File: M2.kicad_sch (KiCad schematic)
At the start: 59 parts, among them J100 Bus_M.2_2199230-2, J6 Bus_M.2_1-2199230-6, Y1 Oscillator_32.768kHz_ECS_2520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

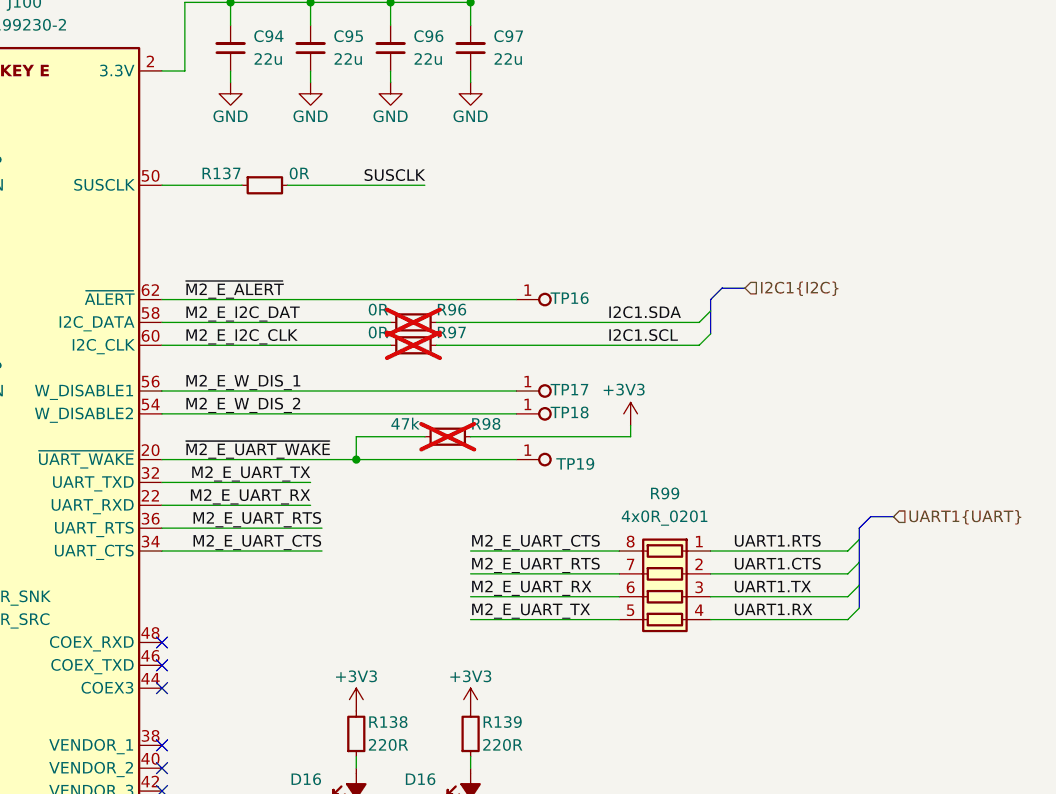
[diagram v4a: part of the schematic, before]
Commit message: [#82048] Beautify M.2 schematic
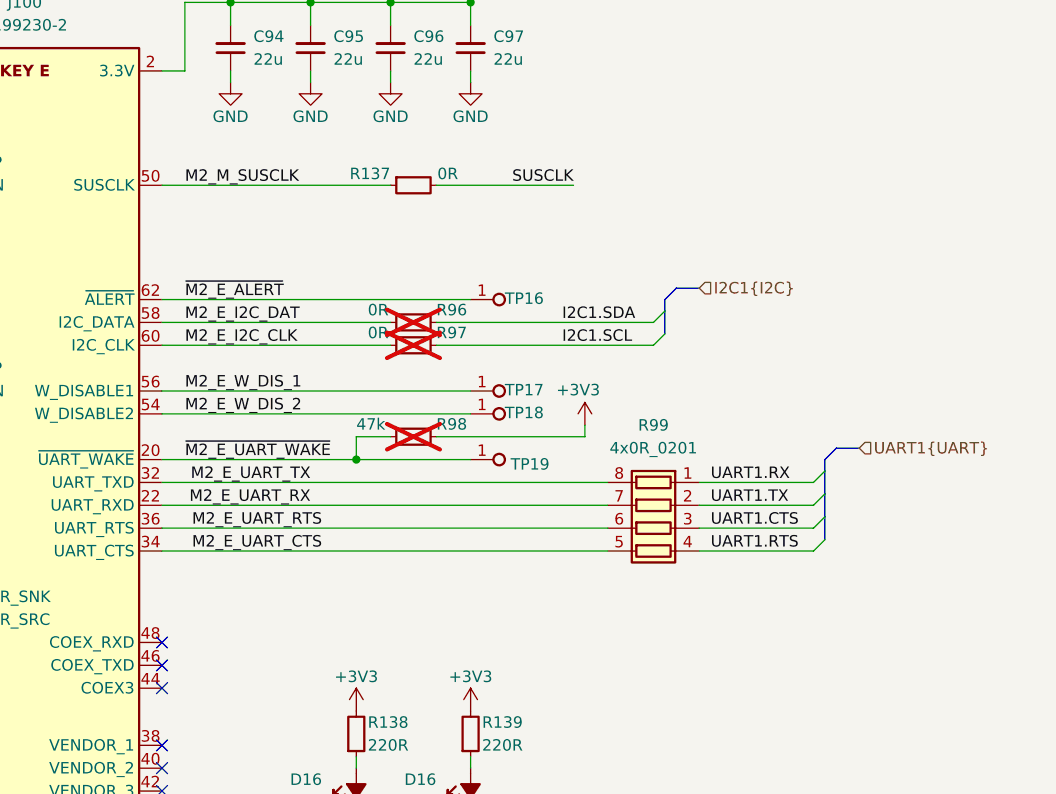
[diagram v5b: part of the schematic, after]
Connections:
- net M2_E_UART_CTS: now also R99.5 (R4.2); no longer R99.8 (R1.2)
- net M2_E_UART_RTS: now also R99.6 (R3.2); no longer R99.7 (R2.2)
- net M2_E_UART_RX: now also R99.7 (R2.2); no longer R99.6 (R3.2)
- net M2_E_UART_TX: now also R99.8 (R1.2); no longer R99.5 (R4.2)
- net M2_M_SUSCLK: now also J100.50 (SUSCLK), R137.1
- net UART1.CTS: now also R99.3 (R3.1); no longer R99.2 (R2.1)
- net UART1.RTS: now also R99.4 (R4.1); no longer R99.1 (R1.1)
- net UART1.RX: now also R99.1 (R1.1); no longer R99.4 (R4.1)
- net UART1.TX: now also R99.2 (R2.1); no longer R99.3 (R3.1)
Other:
- moved on the sheet: R137, R98, R99, TP16, TP17, TP18, TP19

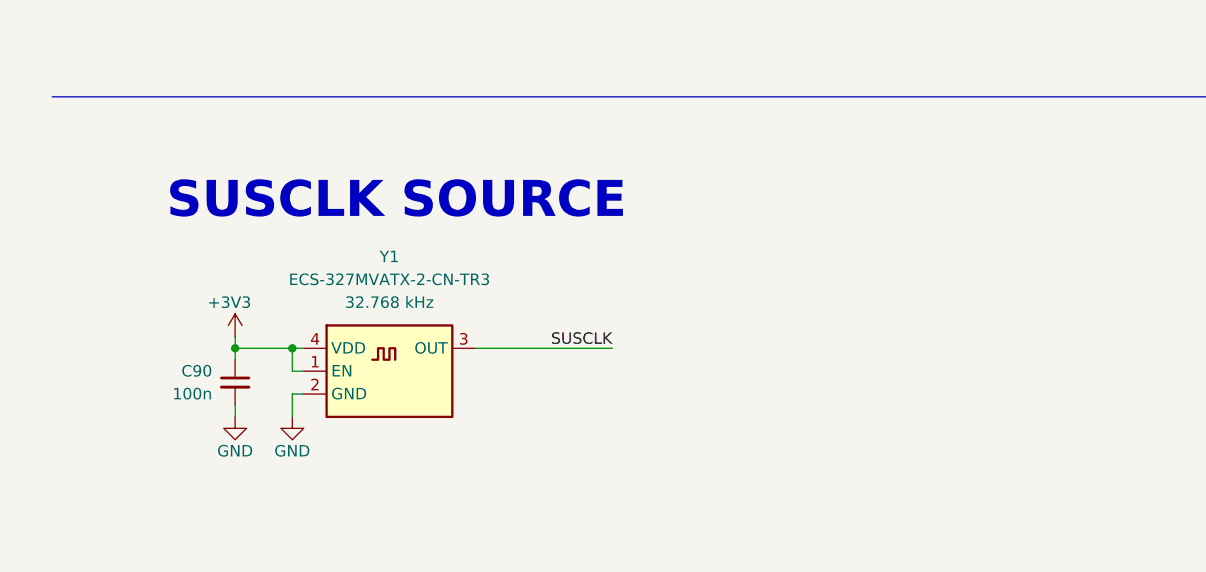
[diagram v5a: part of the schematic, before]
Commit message: [#81970] Connect SFI to SOM
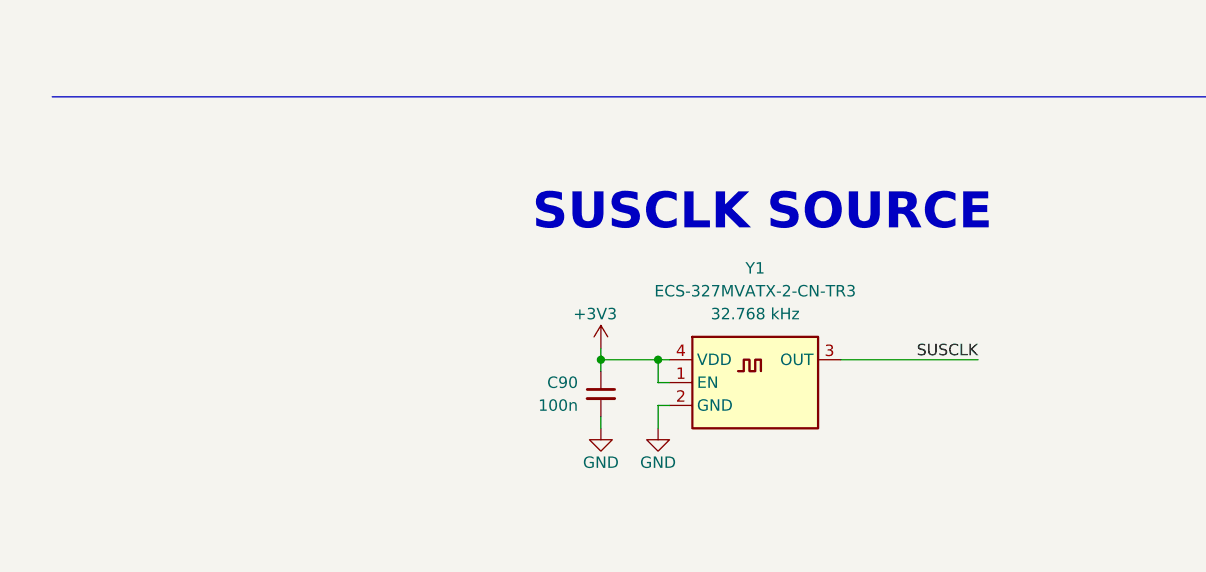
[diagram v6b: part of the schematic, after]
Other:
- moved on the sheet: C90, Y1
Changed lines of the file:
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@@
 	(text "SUSCLK SOURCE"
 		(exclude_from_sim no)
-		(at 25.4 247.65 0)
+		(at 66.04 248.92 0)
 		(effects
 			(font
@@
 	)
 	(junction
-		(at 39.37 261.62)
+		(at 80.01 262.89)
 		(diameter 0)
 		(color 0 0 0 0)
@@
 	)
 	(junction
-		(at 33.02 261.62)
+		(at 73.66 262.89)
 		(diameter 0)
 		(color 0 0 0 0)
@@
 	(wire
 		(pts
-			(xy 40.64 266.7) (xy 39.37 266.7)
+			(xy 81.28 267.97) (xy 80.01 267.97)
 		)
 		(stroke
@@
 	(wire
 		(pts
-			(xy 33.02 261.62) (xy 33.02 260.35)
+			(xy 73.66 262.89) (xy 73.66 261.62)
 		)
 		(stroke
@@
 	(wire
 		(pts
-			(xy 39.37 264.16) (xy 39.37 261.62)
+			(xy 80.01 265.43) (xy 80.01 262.89)
 		)
 		(stroke
@@
 	(wire
 		(pts
-			(xy 74.93 261.62) (xy 59.69 261.62)
+			(xy 115.57 262.89) (xy 100.33 262.89)
 		)
 		(stroke
@@
 	(wire
 		(pts
-			(xy 33.02 261.62) (xy 39.37 261.62)
+			(xy 73.66 262.89) (xy 80.01 262.89)
 		)
 		(stroke
@@
 	(wire
 		(pts
-			(xy 39.37 266.7) (xy 39.37 269.24)
+			(xy 80.01 267.97) (xy 80.01 270.51)
 		)
 		(stroke
@@
 	(wire
 		(pts
-			(xy 39.37 261.62) (xy 40.64 261.62)
+			(xy 80.01 262.89) (xy 81.28 262.89)
 		)
 		(stroke
@@
 	(wire
 		(pts
-			(xy 33.02 267.97) (xy 33.02 269.24)
+			(xy 73.66 269.24) (xy 73.66 270.51)
 		)
 		(stroke
@@
 	(wire
 		(pts
-			(xy 33.02 261.62) (xy 33.02 262.89)
+			(xy 73.66 262.89) (xy 73.66 264.16)
 		)
 		(stroke
@@
 	(wire
 		(pts
-			(xy 40.64 264.16) (xy 39.37 264.16)
+			(xy 81.28 265.43) (xy 80.01 265.43)
 		)
 		(stroke
@@
 	)
 	(label "SUSCLK"
-		(at 74.93 261.62 180)
+		(at 115.57 262.89 180)
 		(effects
 			(font
@@
 	(symbol
 		(lib_id "antmicroOscillators:Oscillator_32.768kHz_ECS_2520MV")
-		(at 40.64 261.62 0)
+		(at 81.28 262.89 0)
 		(unit 1)
 		(exclude_from_sim no)
@@
 		(fields_autoplaced yes)
 		(property "Reference" "Y1"
-			(at 50.165 251.46 0)
+			(at 90.805 252.73 0)
 			(effects
 				(font
@@
 		)
 		(property "Value" "Oscillator_32.768kHz_ECS_2520MV"
-			(at 66.675 274.32 0)
+			(at 107.315 275.59 0)
 			(effects
 				(font
@@
 		)
 		(property "Footprint" "antmicro-footprints:Oscillator_SMD_ECS_2520MV_2.5x2mm"
-			(at 66.675 276.86 0)
+			(at 107.315 278.13 0)
 			(effects
 				(font
@@
 		)
 		(property "Datasheet" "https://ecsxtal.com/store/pdf/ECS-327MVATX.pdf"
-			(at 66.675 279.4 0)
+			(at 107.315 280.67 0)
 			(effects
 				(font
@@
 		)
 		(property "Description" ""
-			(at 40.64 261.62 0)
+			(at 81.28 262.89 0)
 			(effects
 				(font
@@
 		)
 		(property "Manufacturer" "ECS Inc. International"
-			(at 66.675 269.24 0)
+			(at 107.315 270.51 0)
 			(effects
 				(font
@@
 		)
 		(property "MPN" "ECS-327MVATX-2-CN-TR3"
-			(at 50.165 254 0)
+			(at 90.805 255.27 0)
 			(effects
 				(font
@@
 		)
 		(property "Val" "32.768 kHz"
-			(at 50.165 256.54 0)
+			(at 90.805 257.81 0)
 			(effects
 				(font
@@
 		)
 		(property "Author" "Antmicro"
-			(at 66.675 281.94 0)
+			(at 107.315 283.21 0)
 			(effects
 				(font
@@
 		)
 		(property "License" "Apache-2.0"
-			(at 66.675 284.48 0)
+			(at 107.315 285.75 0)
 			(effects
 				(font
@@
 		(lib_name "GND_1")
 		(lib_id "antmicropower:GND")
-		(at 33.02 269.24 0)
+		(at 73.66 270.51 0)
 		(unit 1)
 		(exclude_from_sim no)
@@
 		(dnp no)
 		(property "Reference" "#PWR0137"
-			(at 33.02 275.59 0)
+			(at 73.66 276.86 0)
 			(effects
 				(font
@@
 		)
 		(property "Value" "GND"
-			(at 33.02 273.05 0)
+			(at 73.66 274.32 0)
 			(effects
 				(font
@@
 		)
 		(property "Footprint" ""
-			(at 41.91 276.86 0)
+			(at 82.55 278.13 0)
 			(effects
 				(font
@@
 		)
 		(property "Datasheet" ""
-			(at 41.91 281.94 0)
+			(at 82.55 283.21 0)
 			(effects
 				(font
@@
 		)
 		(property "Description" ""
-			(at 33.02 269.24 0)
+			(at 73.66 270.51 0)
 			(effects
 				(font
@@
 		)
 		(property "Author" "Antmicro"
-			(at 41.91 276.86 0)
+			(at 82.55 278.13 0)
 			(effects
 				(font
@@
 		)
 		(property "License" "Apache-2.0"
-			(at 41.91 279.4 0)
+			(at 82.55 280.67 0)
 			(effects
 				(font
@@
 		(lib_name "GND_2")
 		(lib_id "antmicropower:GND")
-		(at 39.37 269.24 0)
+		(at 80.01 270.51 0)
 		(unit 1)
 		(exclude_from_sim no)
@@
 		(dnp no)
 		(property "Reference" "#PWR0138"
-			(at 39.37 275.59 0)
+			(at 80.01 276.86 0)
 			(effects
 				(font
@@
 		)
 		(property "Value" "GND"
-			(at 39.37 273.05 0)
+			(at 80.01 274.32 0)
 			(effects
 				(font
@@
 		)
 		(property "Footprint" ""
-			(at 48.26 276.86 0)
+			(at 88.9 278.13 0)
 			(effects
 				(font
@@
 		)
 		(property "Datasheet" ""
-			(at 48.26 281.94 0)
+			(at 88.9 283.21 0)
 			(effects
 				(font
@@
 		)
 		(property "Description" ""
-			(at 39.37 269.24 0)
+			(at 80.01 270.51 0)
 			(effects
 				(font
@@
 		)
 		(property "Author" "Antmicro"
-			(at 48.26 276.86 0)
+			(at 88.9 278.13 0)
 			(effects
 				(font
@@
 		)
 		(property "License" "Apache-2.0"
-			(at 48.26 279.4 0)
+			(at 88.9 280.67 0)
 			(effects
 				(font
@@
 		(lib_name "+3V3_1")
 		(lib_id "antmicropower:+3V3")
-		(at 33.02 260.35 0)
+		(at 73.66 261.62 0)
 		(unit 1)
 		(exclude_from_sim no)
@@
 		(dnp no)
 		(property "Reference" "#PWR0136"
-			(at 33.02 264.16 0)
+			(at 73.66 265.43 0)
 			(effects
 				(font
@@
 		)
 		(property "Value" "+3V3"
-			(at 32.385 256.54 0)
+			(at 73.025 257.81 0)
 			(effects
 				(font
@@
 		)
 		(property "Footprint" ""
-			(at 48.26 267.97 0)
+			(at 88.9 269.24 0)
 			(effects
 				(font
@@
 		)
 		(property "Datasheet" ""
-			(at 48.26 270.51 0)
+			(at 88.9 271.78 0)
 			(effects
 				(font
@@
 		)
 		(property "Description" ""
-			(at 33.02 260.35 0)
+			(at 73.66 261.62 0)
 			(effects
 				(font
@@
 		)
 		(property "Author" "Antmicro"
-			(at 48.26 262.89 0)
+			(at 88.9 264.16 0)
 			(effects
 				(font
@@
 		)
 		(property "License" "Apache-2.0"
-			(at 48.26 265.43 0)
+			(at 88.9 266.7 0)
 			(effects
 				(font
@@
 		(lib_name "C_100n_0402_1")
 		(lib_id "antmicroCapacitors0402:C_100n_0402")
-		(at 33.02 262.89 90)
+		(at 73.66 264.16 90)
 		(mirror x)
 		(unit 1)
@@
 		(fields_autoplaced yes)
 		(property "Reference" "C90"
-			(at 30.48 264.1663 90)
+			(at 71.12 265.4363 90)
 			(effects
 				(font
@@
 		)
 		(property "Value" "C_100n_0402"
-			(at 43.18 283.21 0)
+			(at 83.82 284.48 0)
 			(effects
 				(font
@@
 		)
 		(property "Footprint" "antmicro-footprints:C_0402_1005Metric"
-			(at 45.72 283.21 0)
+			(at 86.36 284.48 0)
 			(effects
 				(font
@@
 		)
 		(property "Datasheet" "https://www.murata.com/products/productdetail?partno=GRM155R61H104KE14%23"
-			(at 48.26 283.21 0)
+			(at 88.9 284.48 0)
 			(effects
 				(font
@@
 		)
 		(property "Description" ""
-			(at 33.02 262.89 0)
+			(at 73.66 264.16 0)
 			(effects
 				(font
@@
 		)
 		(property "Manufacturer" "Murata"
-			(at 53.34 283.21 0)
+			(at 93.98 284.48 0)
 			(effects
 				(font
@@
 		)
 		(property "MPN" "GRM155R61H104KE14D"
-			(at 50.8 283.21 0)
+			(at 91.44 284.48 0)
 			(effects
 				(font
@@
 		)
 		(property "Val" "100n"
-			(at 30.48 266.7063 90)
+			(at 71.12 267.9763 90)
 			(effects
 				(font
@@
 		)
 		(property "License" "Apache-2.0"
-			(at 55.88 283.21 0)
+			(at 96.52 284.48 0)
 			(effects
 				(font
@@
 		)
 		(property "Author" "Antmicro"
-			(at 58.42 283.21 0)
+			(at 99.06 284.48 0)
 			(effects
 				(font
@@
 		)
 		(property "Voltage" "50V"
-			(at 60.96 283.21 0)
+			(at 101.6 284.48 0)
 			(effects
 				(font
@@
 		)
 		(property "Dielectric" "X5R"
-			(at 63.5 283.21 0)
+			(at 104.14 284.48 0)
 			(effects
 				(font
